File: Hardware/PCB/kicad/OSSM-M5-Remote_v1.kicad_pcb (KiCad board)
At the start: 2 copper layers, 108.5 x 73.1 mm, 22 parts, among them M5-CORE0 M5_CORE2, U1 PEC12R, U2 PEC12R, U3 PEC12R, U4 PEC12R

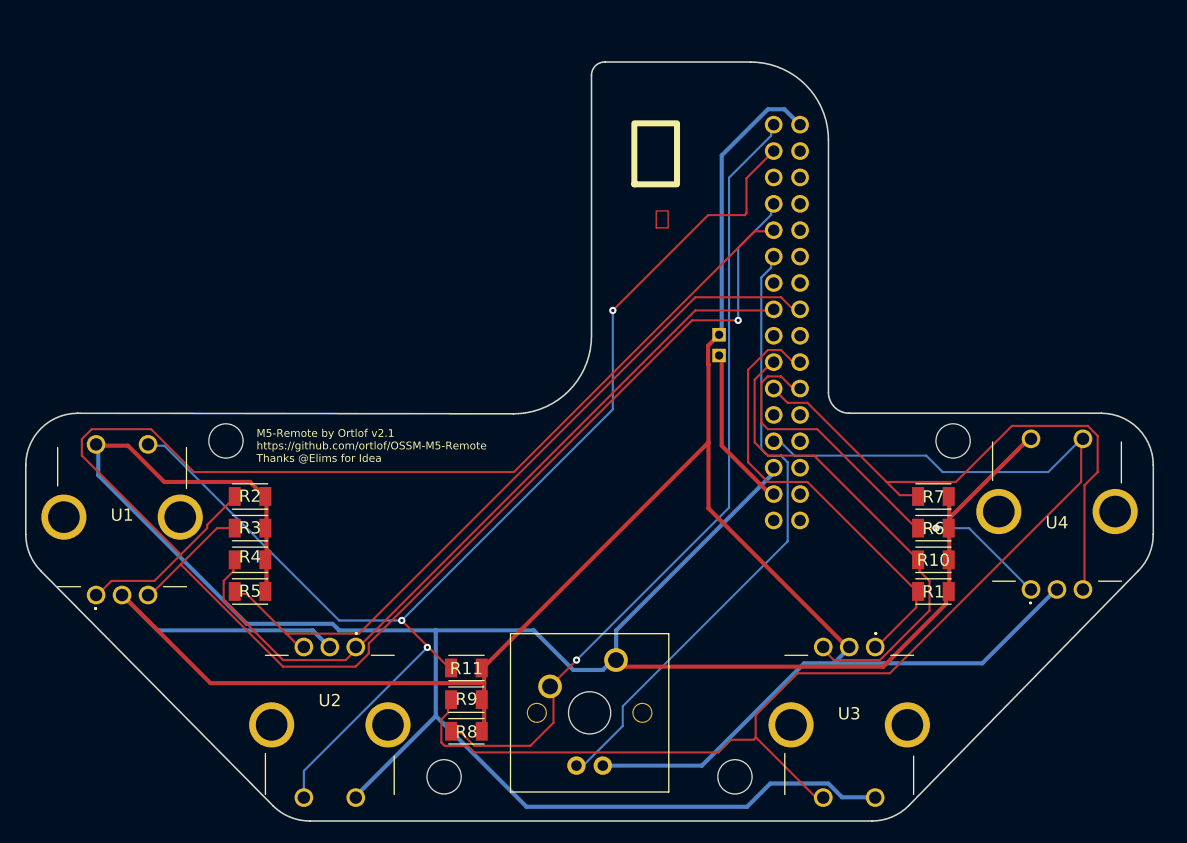
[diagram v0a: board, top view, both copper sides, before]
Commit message: Update schematic, remove traces
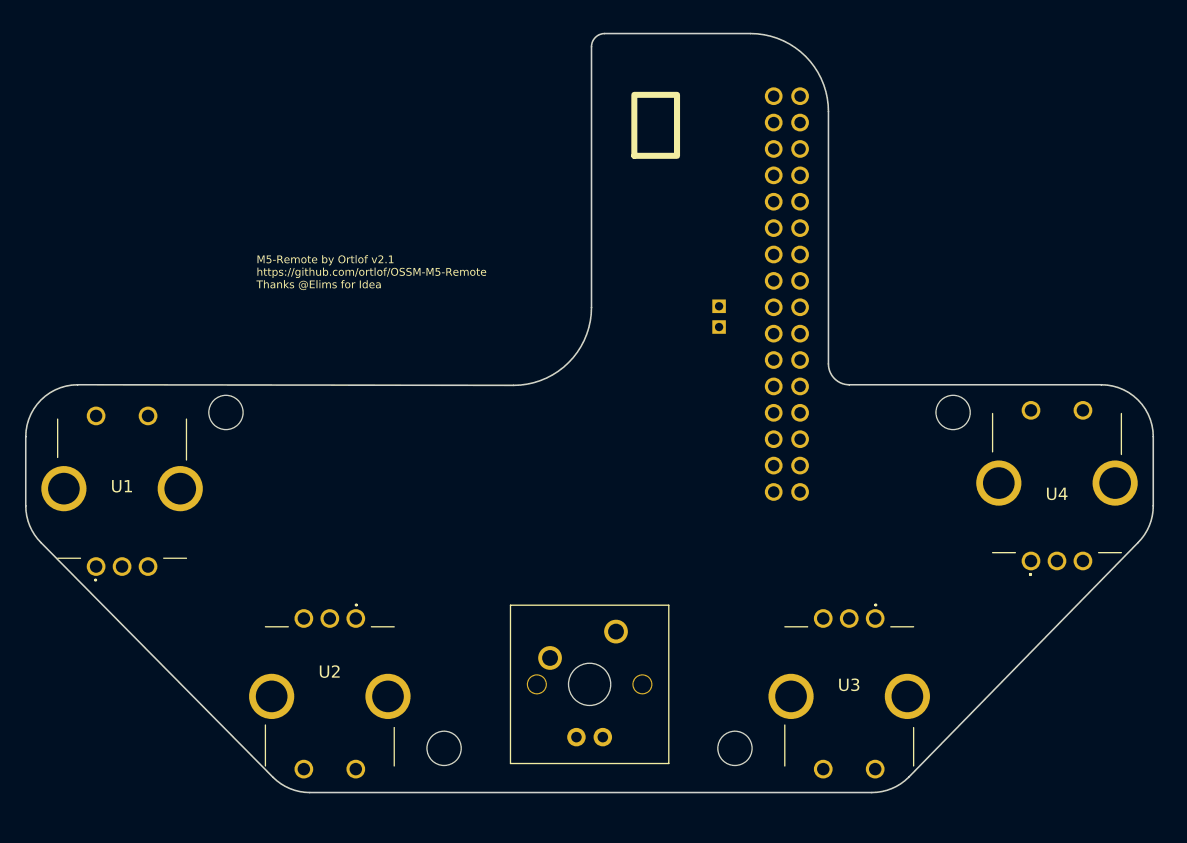
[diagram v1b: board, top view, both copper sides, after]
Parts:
- removed R1, R10, R2, R3, R4, R5, R6, R7, R8, R9: , OSSM-M5-Remote_v1:RESC3216X70
- removed R11: 10k, OSSM-M5-Remote_v1:RESC3216X70
- moved @HOLE0 2.74 mm to (134.5, 134.5)
- moved @HOLE1 2.74 mm to (162.5, 134.5)
- moved M5-CORE0 2.74 mm to (168.8, 107.3)
- moved U$4 2.74 mm to (148.5, 128.4)
- moved U1 2.74 mm to (101.0, 117.0)
- moved U2 2.74 mm to (126.0, 122.0)
- moved U4 2.74 mm to (191.0, 116.5)
- moved @HOLE2 2.74 mm to (113.5, 102.2)
- moved @HOLE3 2.74 mm to (183.5, 102.2)
- moved U$3 2.74 mm to (161.0, 92.0)
- moved U3 2.74 mm to (176.0, 122.0)
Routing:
- net +5V: track 236.5 -> 0.00 mm
- net NEGATIV: track 214.3 -> 0.00 mm
- net N$27: track 124.3 -> 0.00 mm
- net N$26: track 119.6 -> 0.00 mm, vias 3 -> 0
- net N$5: track 110.9 -> 0.00 mm
- net N$6: track 95.8 -> 0.00 mm, vias 1 -> 0
- net N$31: track 78.1 -> 0.00 mm, vias 1 -> 0
- net N$8: track 73.8 -> 0.00 mm
- net N$10: track 72.6 -> 0.00 mm
- net N$3: track 60.2 -> 0.00 mm
- net N$12: track 56.5 -> 0.00 mm
- net N$14: track 47.2 -> 0.00 mm
- net N$13: track 43.8 -> 0.00 mm
- net N$11: track 40.9 -> 0.00 mm, vias 1 -> 0
- net BAT+: track 15.8 -> 0.00 mm
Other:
- board text removed: "Stop looking at my bottom!"

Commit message: updates
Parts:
- removed the U3 at (176.0, 122.0)
- removed U4: PEC12R, OSSM-M5-Remote_v1:PEC12R4017FN0024
- added SW1: ~, OSSM-M5-Remote_v1:PEL12T4225SS1024, F.Cu at (103.5, 109.8)
- added SW2: ~, OSSM-M5-Remote_v1:PEL12T4225SS1024, F.Cu at (123.5, 129.3)
- added SW3: ~, OSSM-M5-Remote_v1:PEL12T4225SS1024, F.Cu at (173.5, 129.3)
- added SW4: ~, OSSM-M5-Remote_v1:PEL12T4225SS1024, F.Cu at (193.5, 109.3)
- U$4: value CHERRY-MX-LED -> Val**
- U1: value PEC12R -> PCA9685PW; footprint OSSM-M5-Remote_v1:PEC12R4017FN0024 -> Package_SO:TSSOP-28_4.4x9.7mm_P0.65mm
- U2: value PEC12R -> MCP23017_SS; footprint OSSM-M5-Remote_v1:PEC12R4017FN0024 -> Package_SO:SSOP-28_5.3x10.2mm_P0.65mm
- moved U1 38.9 mm to (139.4, 110.9)
- moved U2 31.0 mm to (154.9, 110.8), turned to 0 degrees
- renumbered M5-CORE0 to M5-CORE2, U$3 to U3
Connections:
- M5-CORE2 pad 1: (no net) -> unconnected-(M5-CORE2-NC-Pad1)
- M5-CORE2 pad 10: (no net) -> unconnected-(M5-CORE2-G18-Pad10)
- M5-CORE2 pad 11: (no net) -> unconnected-(M5-CORE2-G38-Pad11)
- M5-CORE2 pad 12: (no net) -> unconnected-(M5-CORE2-G23-Pad12)
- M5-CORE2 pad 13: (no net) -> GND
- M5-CORE2 pad 14: (no net) -> GND
- M5-CORE2 pad 15: NEGATIV -> GND
- M5-CORE2 pad 16: N$31 -> unconnected-(M5-CORE2-G35-Pad16)
- M5-CORE2 pad 17: N$26 -> unconnected-(M5-CORE2-G36-Pad17)
- M5-CORE2 pad 18: (no net) -> unconnected-(M5-CORE2-RST-Pad18)
- M5-CORE2 pad 19: N$6 -> unconnected-(M5-CORE2-G25-Pad19)
- M5-CORE2 pad 2: (no net) -> unconnected-(M5-CORE2-NC-Pad2)
- M5-CORE2 pad 20: N$5 -> unconnected-(M5-CORE2-G26-Pad20)
- M5-CORE2 pad 21: N$3 -> +3.3V
- M5-CORE2 pad 22: (no net) -> unconnected-(M5-CORE2-G1-Pad22)
- M5-CORE2 pad 23: N$8 -> unconnected-(M5-CORE2-G14-Pad23)
- M5-CORE2 pad 24: (no net) -> unconnected-(M5-CORE2-G22-Pad24)
- M5-CORE2 pad 25: N$14 -> /SCL
- M5-CORE2 pad 26: N$12 -> /INTA
- M5-CORE2 pad 27: (no net) -> unconnected-(M5-CORE2-G0-Pad27)
- M5-CORE2 pad 28: N$27 -> unconnected-(M5-CORE2-G34-Pad28)
- M5-CORE2 pad 3: (no net) -> unconnected-(M5-CORE2-NC-Pad3)
- M5-CORE2 pad 30: BAT+ -> +BATT
- M5-CORE2 pad 4: (no net) -> unconnected-(M5-CORE2-G2-Pad4)
- M5-CORE2 pad 5: N$11 -> /INTB
- M5-CORE2 pad 6: N$13 -> /SDA
- M5-CORE2 pad 7: (no net) -> unconnected-(M5-CORE2-G21-Pad7)
- M5-CORE2 pad 8: N$10 -> unconnected-(M5-CORE2-G13-Pad8)
- M5-CORE2 pad 9: (no net) -> unconnected-(M5-CORE2-G3-Pad9)
- U$4 pad LED+: N$3 -> +5V
- U$4 pad LED-: NEGATIV -> Net-(R7-Pad1)
- U$4 pad SW1: N$31 -> GND
- U$4 pad SW2: +5V -> Net-(U2-GPB6)

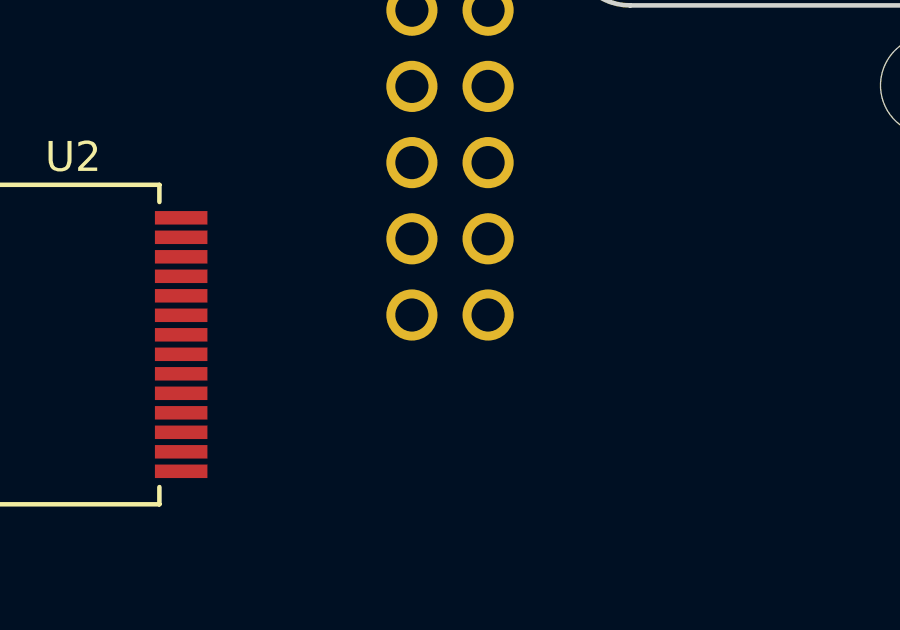
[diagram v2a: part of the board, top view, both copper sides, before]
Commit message: Cleaner schematic
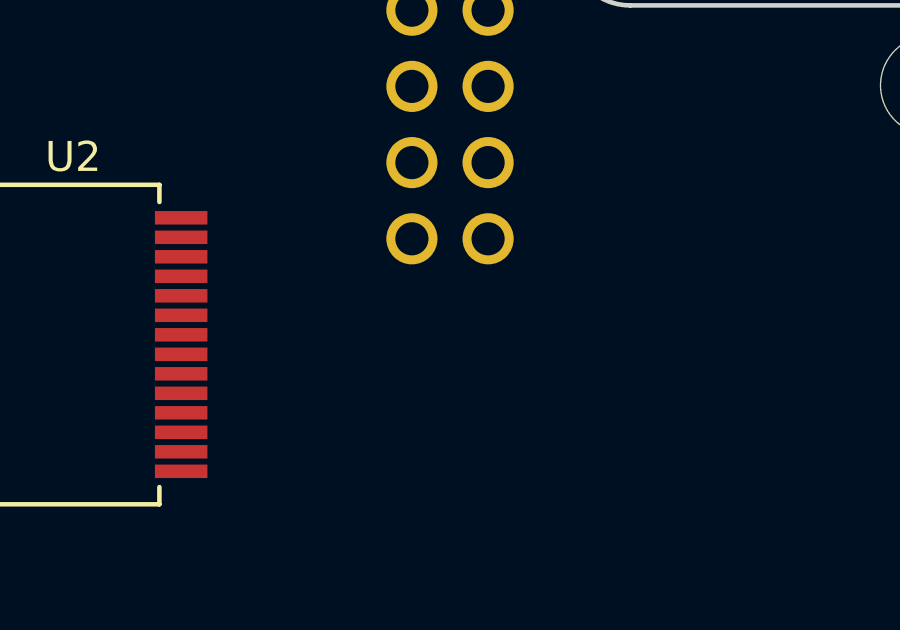
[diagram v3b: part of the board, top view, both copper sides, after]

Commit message: Starting routing
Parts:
- added C1: 100n, Capacitor_SMD:C_0402_1005Metric, B.Cu at (138.0, 113.7)
- added C2: 100n, Capacitor_SMD:C_0402_1005Metric, B.Cu at (144.5, 107.8)
- added R1: 120R, Resistor_SMD:R_0603_1608Metric, B.Cu at (118.8, 118.2)
- added R10: 120R, Resistor_SMD:R_0603_1608Metric, B.Cu at (162.2, 124.2)
- added R11: 120R, Resistor_SMD:R_0603_1608Metric, B.Cu at (162.2, 126.8)
- added R12: 4k7, Resistor_SMD:R_0603_1608Metric, B.Cu at (162.2, 129.3)
- added R13: 120R, Resistor_SMD:R_0603_1608Metric, B.Cu at (181.0, 108.0)
- added R14: 120R, Resistor_SMD:R_0603_1608Metric, B.Cu at (181.0, 110.2)
- added R15: 120R, Resistor_SMD:R_0603_1608Metric, B.Cu at (181.1, 112.5)
- added R16: 4k7, Resistor_SMD:R_0603_1608Metric, B.Cu at (168.5, 113.0)
- added R17: 120R, Resistor_SMD:R_0603_1608Metric, B.Cu at (137.9, 126.2)
- added R18: 4k7, Resistor_SMD:R_0603_1608Metric, B.Cu at (160.5, 99.2)
- added R19: 4k7, Resistor_SMD:R_0603_1608Metric, B.Cu at (162.8, 99.2)
- added R2: 120R, Resistor_SMD:R_0603_1608Metric, B.Cu at (117.0, 118.2)
- added R3: 120R, Resistor_SMD:R_0603_1608Metric, B.Cu at (115.2, 118.2)
- added R4: 4k7, Resistor_SMD:R_0603_1608Metric, B.Cu at (134.1, 123.0)
- added R5: 120R, Resistor_SMD:R_0603_1608Metric, B.Cu at (115.8, 113.2)
- added R6: 120R, Resistor_SMD:R_0603_1608Metric, B.Cu at (115.8, 111.5)
- added R7: 120R, Resistor_SMD:R_0603_1608Metric, B.Cu at (115.8, 106.0)
- added R8: 4k7, Resistor_SMD:R_0603_1608Metric, B.Cu at (115.8, 108.8)
- added R9: 120R, Resistor_SMD:R_0603_1608Metric, B.Cu at (161.9, 120.8)
- H1: renamed from @HOLE1; value (none) -> MountingHole; footprint (none) -> OSSM-M5-Remote_v1:mounting_hole_3.3mm
- H2: renamed from @HOLE2; value (none) -> MountingHole; footprint (none) -> OSSM-M5-Remote_v1:mounting_hole_3.3mm
- H3: renamed from @HOLE3; value (none) -> MountingHole; footprint (none) -> OSSM-M5-Remote_v1:mounting_hole_3.3mm
- H4: renamed from @HOLE0; value (none) -> MountingHole; footprint (none) -> OSSM-M5-Remote_v1:mounting_hole_3.3mm
- U1, U2: moved to B.Cu
- U4: renamed from U$4; value Val** -> CHERRY-MX-LED
- moved U1 6.42 mm to (133.2, 109.0)
- moved U2 5.27 mm to (150.0, 109.0)
- renumbered SW2 to SW1, SW1 to SW2
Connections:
- net Net-(SW3-SW) renamed /SW3_BUTTON
- net Net-(SW4-SW) renamed /SW4_BUTTON
- net Net-(U2-GPB6) renamed /CHERRY_BUTTON
- M5-CORE2 pad 26: /INTA -> /INTB
- M5-CORE2 pad 5: /INTB -> /INTA
- SW1 pad 1: Net-(SW2--R) -> /LEDD_SW1_R
- SW1 pad 2: Net-(SW2--G) -> /LEDD_SW1_G
- SW1 pad 3: /SW2_BUTTON -> /SW1_BUTTON
- SW1 pad 4: Net-(SW2--B) -> /LEDD_SW1_B
- SW1 pad A: (no net) -> /SW1_ROTA
- SW1 pad B: (no net) -> /SW1_ROTB
- SW1 pad C: (no net) -> GND
- SW1 pad MH1: (no net) -> GND
- SW1 pad MH2: (no net) -> GND
- SW2 pad 1: Net-(SW1--R) -> /LEDD_SW2_R
- SW2 pad 2: Net-(SW1--G) -> /LEDD_SW2_G
- SW2 pad 3: /SW1_BUTTON -> /SW2_BUTTON
- SW2 pad 4: Net-(SW1--B) -> /LEDD_SW2_B
- SW2 pad A: (no net) -> /SW2_ROTB
- SW2 pad B: (no net) -> /SW2_ROTA
- SW2 pad C: (no net) -> GND
- SW2 pad MH1: (no net) -> GND
- SW2 pad MH2: (no net) -> GND
- SW3 pad 1: Net-(SW3--R) -> /LEDD_SW3_R
- SW3 pad 2: Net-(SW3--G) -> /LEDD_SW3_G
- SW3 pad 4: Net-(SW3--B) -> /LEDD_SW3_B
- SW3 pad A: (no net) -> /SW3_ROTB
- SW3 pad B: (no net) -> /SW3_ROTA
- SW3 pad C: (no net) -> GND
- SW3 pad MH1: (no net) -> GND
- SW3 pad MH2: (no net) -> GND
- SW4 pad 1: Net-(SW4--R) -> /LEDD_SW4_R
- SW4 pad 2: Net-(SW4--G) -> /LEDD_SW4_G
- SW4 pad 4: Net-(SW4--B) -> /LEDD_SW4_B
- SW4 pad A: (no net) -> /SW4_ROTA
- SW4 pad B: (no net) -> /SW4_ROTB
- SW4 pad C: (no net) -> GND
- SW4 pad MH1: (no net) -> GND
- SW4 pad MH2: (no net) -> GND
- U1 pad 10: Net-(U1-LED4) -> /LED_SW2_G
- U1 pad 11: Net-(U1-LED5) -> /LED_SW2_B
- U1 pad 12: Net-(U1-LED6) -> /LED_CHERRY
- U1 pad 15: Net-(U1-LED8) -> /LED_SW4_R
- U1 pad 16: Net-(U1-LED9) -> /LED_SW4_G
- U1 pad 17: Net-(U1-LED10) -> /LED_SW4_B
- U1 pad 18: Net-(U1-LED11) -> /LED_SW3_R
- U1 pad 19: Net-(U1-LED12) -> /LED_SW3_G
- U1 pad 20: Net-(U1-LED13) -> /LED_SW3_B
- U1 pad 6: Net-(U1-LED0) -> /LED_SW1_R
- U1 pad 7: Net-(U1-LED1) -> /LED_SW1_G
- U1 pad 8: Net-(U1-LED2) -> /LED_SW1_B
- U1 pad 9: Net-(U1-LED3) -> /LED_SW2_R
- U2 pad 1: Net-(U2-GPB0) -> /SW1_ROTA
- U2 pad 2: Net-(U2-GPB1) -> /SW1_ROTB
- U2 pad 22: Net-(U2-GPA1) -> /SW4_ROTB
- U2 pad 23: Net-(U2-GPA2) -> /SW4_ROTA
- U2 pad 25: Net-(U2-GPA4) -> /SW3_ROTB
- U2 pad 26: Net-(U2-GPA5) -> /SW3_ROTA
- U2 pad 4: Net-(U2-GPB3) -> /SW2_ROTA
- U2 pad 5: Net-(U2-GPB4) -> /SW2_ROTB
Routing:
- net +5V: track 0.00 -> 71.3 mm
- net GND: track 0.00 -> 26.0 mm, vias 0 -> 11
- net /LEDD_SW2_R: track 0.00 -> 22.2 mm
- net /SW4_BUTTON: track 0.00 -> 21.9 mm
- net /LEDD_SW1_R: track 0.00 -> 21.1 mm
- net /LEDD_SW1_G: track 0.00 -> 21.0 mm
- net /LEDD_SW2_G: track 0.00 -> 20.9 mm
- net /LEDD_SW4_B: track 0.00 -> 20.7 mm
- net /LEDD_SW1_B: track 0.00 -> 20.1 mm
- net /SCL: track 0.00 -> 20.0 mm
- net /LED_SW1_B: track 0.00 -> 18.8 mm
- net +BATT: track 0.00 -> 16.8 mm
- net /LED_SW1_G: track 0.00 -> 16.7 mm
- net /LED_SW2_R: track 0.00 -> 16.0 mm
- net /LED_SW2_G: track 0.00 -> 15.5 mm
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- added copper zone on F.Cu, net GND

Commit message: Everything connected
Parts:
- R1, R10, R11, R12, R13, R14, R15, R16, R17, R18, R19, R2, R3, R4, R5, R6, R7, R8, R9: footprint Resistor_SMD:R_0603_1608Metric -> Resistor_SMD:R_1206_3216Metric
- moved R4 17.6 mm to (117.2, 117.8), turned to 90 degrees
- moved R16 12.5 mm to (181.0, 112.5), turned to 180 degrees
- moved R19 7.03 mm to (155.8, 98.5), turned to -90 degrees
- moved R1 3.53 mm to (122.2, 117.8)
- moved R2 2.79 mm to (119.8, 117.8)
- moved R12 2.51 mm to (162.2, 126.8)
- moved R18 2.40 mm to (162.8, 100.0)
- moved R15 2.25 mm to (181.0, 114.8)
- moved R11 2.25 mm to (162.2, 129.0)
- moved R17 1.19 mm to (139.0, 126.8), turned to 90 degrees
- moved R9 1.04 mm to (162.2, 121.8)
- moved R6 0.75 mm to (115.7, 110.8)
- moved R3 0.68 mm to (114.8, 117.8)
- moved R13 0.49 mm to (181.0, 107.5)
- moved R8 0.26 mm to (115.8, 108.5), turned to 0 degrees
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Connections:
- SW3 pad A: /SW3_ROTB -> /SW3_ROTA
- SW3 pad B: /SW3_ROTA -> /SW3_ROTB
- U2 pad 24: /SW3_BUTTON -> /SW3_ROTA
- U2 pad 26: /SW3_ROTA -> /SW3_BUTTON
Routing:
- net +5V: track 71.3 -> 350.0 mm, vias 0 -> 3
- net /SW1_BUTTON: track 0.00 -> 52.1 mm
- net /SW2_BUTTON: track 11.6 -> 61.0 mm
- net /SW2_ROTB: track 0.00 -> 49.2 mm
- net /LED_SW4_R: track 0.00 -> 47.8 mm, vias 0 -> 2
- net /LED_SW4_B: track 0.00 -> 47.0 mm, vias 0 -> 2
- net /LED_SW4_G: track 0.00 -> 47.0 mm, vias 0 -> 2
- net /SW4_ROTB: track 0.00 -> 46.6 mm
- net /SDA: track 7.57 -> 52.6 mm
- net /SW2_ROTA: track 0.00 -> 43.2 mm
- net /SW4_ROTA: track 0.00 -> 40.9 mm
- net /SW3_BUTTON: track 0.00 -> 38.8 mm
- net /LED_SW3_B: track 0.00 -> 35.6 mm, vias 0 -> 2
- net /LED_SW3_G: track 0.00 -> 31.7 mm, vias 0 -> 2
- net /LED_SW3_R: track 0.00 -> 30.9 mm, vias 0 -> 2
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
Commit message: PCB updates
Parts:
- added B2: ~, Connector_JST:JST_PH_S2B-PH-K_1x02_P2.00mm_Horizontal, B.Cu at (161.0, 80.2)
- B1: renamed from U3; footprint OSSM-M5-Remote_v1:JST-PH-2.0MM_180DEGREES -> Connector_JST:JST_PH_S2B-PH-K_1x02_P2.00mm_Horizontal
- U4: value CHERRY-MX-LED -> Val**
- moved B1 2.48 mm to (161.0, 89.5), turned to 90 degrees
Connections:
- net Net-(R17-Pad1) renamed /LEDD_CHERRY
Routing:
- net +BATT: track 16.8 -> 33.6 mm
- net +5V: track 350.0 -> 353.8 mm
- net /SDA: track 52.6 -> 51.8 mm
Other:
- board text added: "Do look at my bottom :)"
- board text added: "Don't forget to floss"
- board text added: "I2C Addresses: MCP23017 - 0x21 PCA9685 - 0x42"
- board text added: "M5-Remote https://github.com/erotronik/M5-Remote Based on M5-Remote by Ortlof"
- board text added: "Only populate one battery connector"
- board text removed: "M5-Remote by Ortlof v2.1 https://github.com/ortlof/OSSM-M5-Remote Thanks @Elims for Idea"
